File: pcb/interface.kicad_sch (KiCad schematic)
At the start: 22 parts

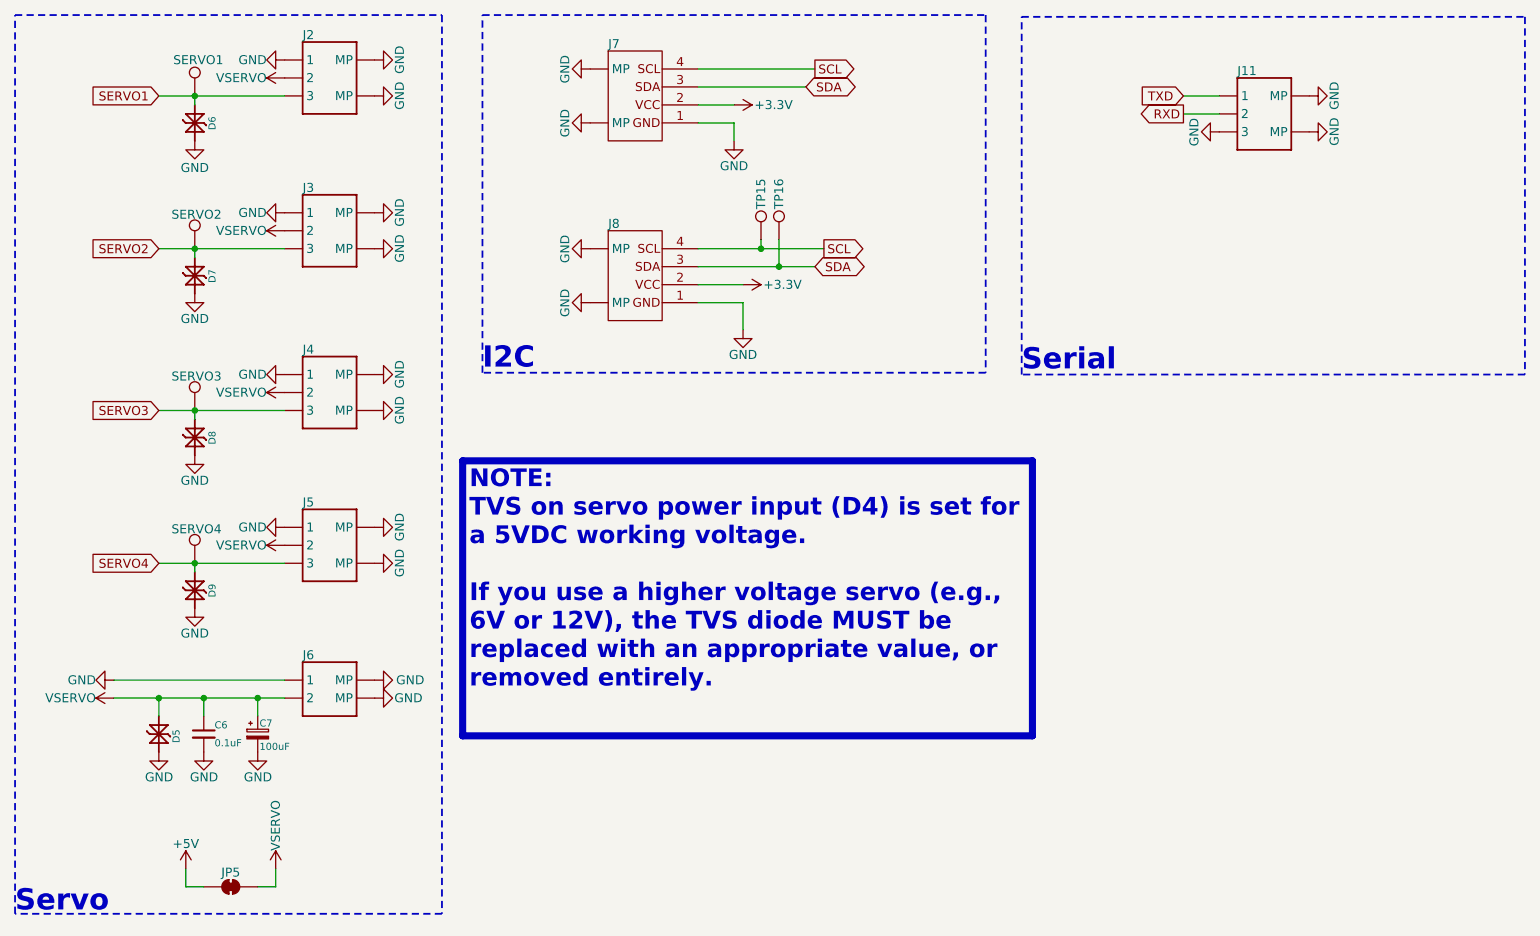
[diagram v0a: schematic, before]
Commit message: Added guard ring
Optimized layout
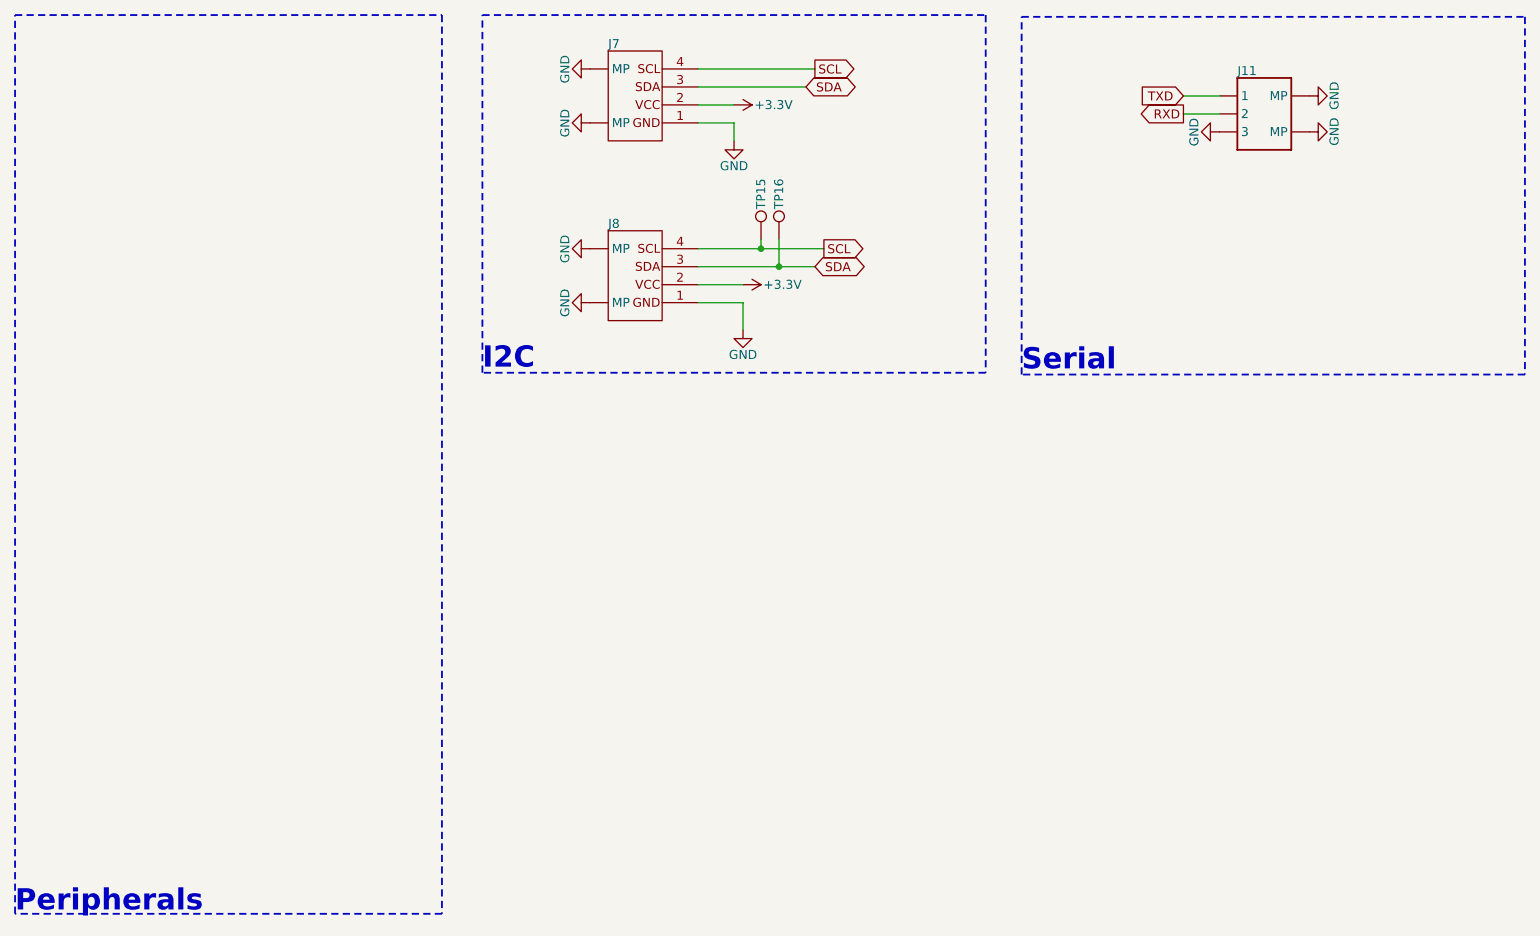
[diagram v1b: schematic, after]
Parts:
- removed C6: 0.1uF, CRGM Passive:C_0603_1608Metric, symbol Device:C_Small
- removed C7: 100uF, CRGM Passive:CP_Elec_5x5.4, symbol CRGM Passive:C_Polarized_Small
- removed D5: PESD5V5C1BL, CRGM Passive:DFN1006-2, symbol CRGM Passive:PESD5V5C1BLYL
- removed D6, D7, D8, D9: PESD3V3S1BL, CRGM Passive:DFN1006-2, symbol CRGM Passive:PESD3V3S1BL
- removed J2, J3, J4, J5: ~, CRGM Connector:JST_SH_BM03B-SRSS-TB_1x03-1MP_P1.00mm_Vertical, symbol CRGM Connector:JST-SH-3
- removed J6: ~, CRGM Connector:JST_SH_BM02B-SRSS-TB_1x02-1MP_P1.00mm_Vertical, symbol CRGM Connector:JST-SH-2
- removed JP5: ~, CRGM Connector:SolderJumper-2_P2.0mm_Bridged_RoundedPad1.0x1.5mm, symbol Jumper:SolderJumper_2_Bridged
- removed TP11: SERVO1, CRGM Mechanical:TestPoint_Pad_D1.0mm, symbol Connector:TestPoint
- removed TP12: SERVO2, CRGM Mechanical:TestPoint_Pad_D1.0mm, symbol Connector:TestPoint
- removed TP13: SERVO3, CRGM Mechanical:TestPoint_Pad_D1.0mm, symbol Connector:TestPoint
- removed TP14: SERVO4, CRGM Mechanical:TestPoint_Pad_D1.0mm, symbol Connector:TestPoint
- J11, J7, J8, TP15, TP16: value ~ -> (none)
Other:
- note added: "Peripherals"
- note removed: "Servo"
